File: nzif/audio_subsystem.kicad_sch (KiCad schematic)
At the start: 21 parts, among them J3 AudioJack3, U20 ADAU1761BCPZ, X1 ASE-12.288MHz

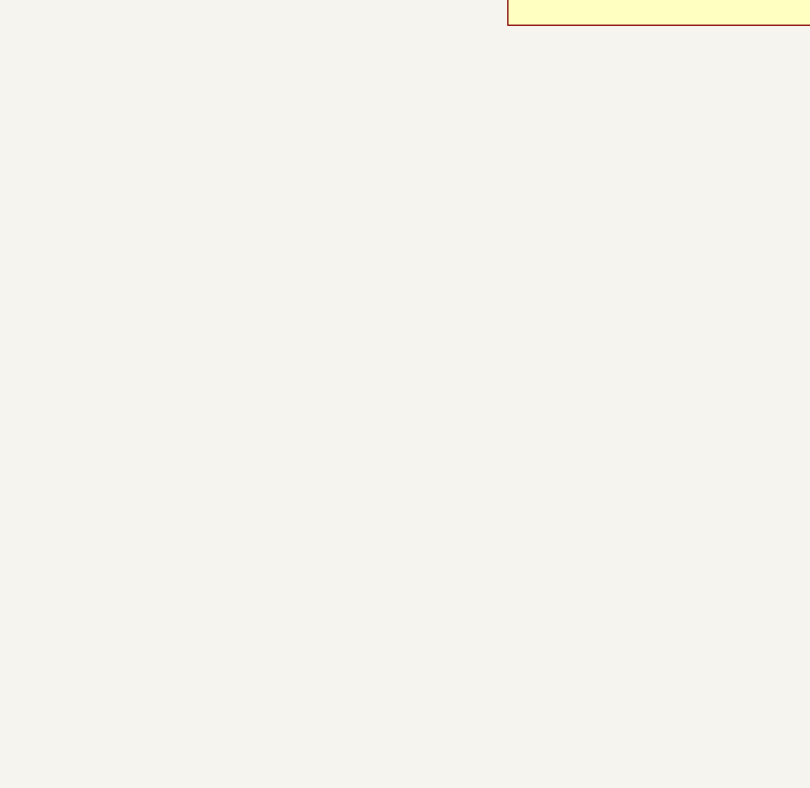
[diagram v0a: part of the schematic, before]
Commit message: add klc compliant 1761
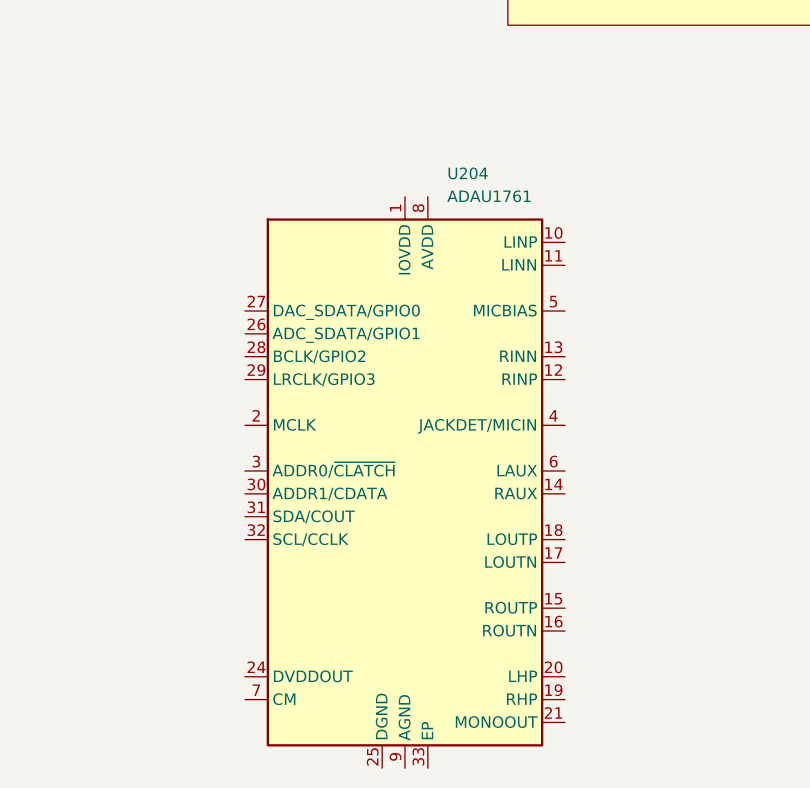
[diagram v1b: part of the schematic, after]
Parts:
- added U204: ADAU1761, Package_CSP:LFCSP-32-1EP_5x5mm_P0.5mm_EP3.5x3.5mm_ThermalVias, symbol Audio:ADAU1761
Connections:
- new net: U204.22 (AGND), U204.9 (AGND)
- new net: U204.23 (AVDD), U204.8 (AVDD)
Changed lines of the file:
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@@
+	)
+	(symbol
+		(lib_id "Audio:ADAU1761")
+		(at 219.71 191.77 0)
+		(unit 1)
+		(exclude_from_sim no)
+		(in_bom yes)
+		(on_board yes)
+		(dnp no)
+		(fields_autoplaced yes)
+		(property "Reference" "U204"
+			(at 224.3933 158.75 0)
+			(effects
+				(font
+					(size 1.27 1.27)
+				)
+				(justify left)
+			)
+		)
+		(property "Value" "ADAU1761"
+			(at 224.3933 161.29 0)
+			(effects
+				(font
+					(size 1.27 1.27)
+				)
+				(justify left)
+			)
+		)
+		(property "Footprint" "Package_CSP:LFCSP-32-1EP_5x5mm_P0.5mm_EP3.5x3.5mm_ThermalVias"
+			(at 219.71 232.918 0)
+			(effects
+				(font
+					(size 1.27 1.27)
+				)
+				(hide yes)
+			)
+		)
+		(property "Datasheet" "https://www.analog.com/media/en/technical-documentation/data-sheets/ADAU1761.pdf"
+			(at 219.71 230.886 0)
+			(effects
+				(font
+					(size 1.27 1.27)
+				)
+				(hide yes)
+			)
+		)
+		(property "Description" "SigmaDSP Stereo, Low Power, 96 kHz, 24-bit Audio Codec with Integrated PLL, VQFN-32 (LFCSP-32)"
+			(at 219.71 228.854 0)
+			(effects
+				(font
+					(size 1.27 1.27)
+				)
+				(hide yes)
+			)
+		)
+		(pin "29"
+		)
+		(pin "3"
+		)
+		(pin "26"
+		)
+		(pin "31"
+		)
+		(pin "28"
+		)
+		(pin "2"
+		)
+		(pin "27"
+		)
+		(pin "30"
+		)
+		(pin "12"
+		)
+		(pin "6"
+		)
+		(pin "22"
+		)
+		(pin "32"
+		)
+		(pin "25"
+		)
+		(pin "1"
+		)
+		(pin "9"
+		)
+		(pin "8"
+		)
+		(pin "11"
+		)
+		(pin "5"
+		)
+		(pin "7"
+		)
+		(pin "24"
+		)
+		(pin "23"
+		)
+		(pin "33"
+		)
+		(pin "10"
+		)
+		(pin "13"
+		)
+		(pin "4"
+		)
+		(pin "17"
+		)
+		(pin "18"
+		)
+		(pin "15"
+		)
+		(pin "16"
+		)
+		(pin "20"
+		)
+		(pin "14"
+		)
+		(pin "21"
+		)
+		(pin "19"
+		)
+		(instances
+			(project ""
+				(path "/fe42ca2f-2bb8-4d5a-9e84-807788ed632f/91ace161-62c2-4ad0-a80e-f8c3c9bc5e50"
+					(reference "U204")
+					(unit 1)
+				)
+			)
+		)
 	)
 	(symbol

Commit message: updated audio subsystem
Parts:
- removed C62, C63, C65, C66, C68, C70: 10u, Capacitor_SMD:C_0805_2012Metric_Pad1.18x1.45mm_HandSolder, symbol Device:C_Polarized_Small_US
- removed C64, C67, C69, C77, C78: 0.1u, Capacitor_SMD:C_0805_2012Metric_Pad1.18x1.45mm_HandSolder, symbol Device:C_Small
- removed C79: 9.1p, Capacitor_SMD:C_0805_2012Metric_Pad1.18x1.45mm_HandSolder, symbol Device:C_Small
- removed C81, C82, C85, C86: 10u, Capacitor_SMD:C_0805_2012Metric_Pad1.18x1.45mm_HandSolder, symbol Device:C_Small
- removed J3: AudioJack3, Connector_Audio:Jack_3.5mm_CUI_SJ-3523-SMT_Horizontal, symbol Connector:AudioJack3
- removed L3: 1.2n, Inductor_SMD:L_0805_2012Metric_Pad1.15x1.40mm_HandSolder, symbol Device:L_Small
- removed R25: 49.9, Resistor_SMD:R_0805_2012Metric_Pad1.20x1.40mm_HandSolder, symbol Device:R_Small_US
- removed U20: ADAU1761BCPZ, Package_DFN_QFN:QFN-32-1EP_5x5mm_P0.5mm_EP3.45x3.45mm, symbol ADAU1761:ADAU1761BCPZ
- removed U204: ADAU1761, Package_CSP:LFCSP-32-1EP_5x5mm_P0.5mm_EP3.5x3.5mm_ThermalVias, symbol Audio:ADAU1761
- removed X1: ASE-12.288MHz, Oscillator:Oscillator_SMD_Abracon_ASE-4Pin_3.2x2.5mm, symbol Oscillator:ASE-xxxMHz
- added C1, C10, C12, C3, C5, C7: 10u, symbol Device:C_Small
- added C11, C15, C16, C2, C4, C6, C8: 0.1u, symbol Device:C_Small
- added C13, C9: 220u, symbol Device:C_Polarized
- added C14: 0.47u, symbol Device:C_Small
- added R1, R4: 49.9k, symbol Device:R_Small_US
- added R2, R6: 10k, symbol Device:R_Small_US
- added R3: 2k, symbol Device:R_Small_US
- added R5: 1k, symbol Device:R_Small_US
- added U1: ADAU1361, Package_CSP:LFCSP-32-1EP_5x5mm_P0.5mm_EP3.5x3.5mm_ThermalVias, symbol Audio:ADAU1361
- added U2: SSM2211S, Package_SO:SOIC-8_3.9x4.9mm_P1.27mm, symbol Amplifier_Audio:SSM2211S
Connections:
- net GND: now also C1.2, C11.1, C15.2, C16.2, C2.2, C3.2, C4.2, C5.2, C6.2, C7.2, C8.2, R1.2, R4.2, U1.22 (AGND), U1.25 (DGND), U1.3 (ADDR0/~{CLATCH}), U1.30 (ADDR1/CDATA), U1.33 (EP), U1.9 (AGND), U2.7 (V-)
- new net: C10.1, U1.11 (LINN)
- new net: C13.1, U1.19 (RHP)
- new net: C14.1, U1.21 (MONOOUT)
- new net: C14.2, R2.1
- new net: C16.1, U2.2 (BYPASS), U2.3 (IN+)
- new net: R2.2, R6.1, U2.4 (IN-)
- new net: C12.1, U1.6 (LAUX)
- new net: C12.2, R4.1, R5.1
- new net: C9.1, U1.20 (LHP)
- new net 3.3V_CODEC: C1.1, C2.1, C3.1, C4.1, U1.1 (IOVDD), U1.23 (AVDD), U1.8 (AVDD)
- new net 5V_Amp: C15.1, U2.6 (V+)
- new net ADC_SDATA: U1.26 (ADC_SDATA)
- new net AMP_SHUTDOWN: U2.1 (SHUTDOWN)
- new net BCLK: U1.28 (BCLK)
- new net CM: C7.1, C8.1, U1.10 (LINP), U1.7 (CM)
- new net DAC_SDATA: U1.27 (DAC_SDATA)
- new net DVDOUT: C5.1, C6.1, U1.24 (DVDDOUT)
- new net Headphone_L: C9.2
- new net Headphone_R: C13.2
- new net LRCLK: U1.29 (LRCLK), U1.32 (SCL/CCLK)
- new net Line_Input: R5.2
- new net Line_Input_ROUTN: U1.16 (ROUTN)
- new net Line_Input_ROUTP: U1.15 (ROUTP)
- new net MCLK: U1.2 (MCLK), U1.31 (SDA/COUT)
- new net MICBIAS: C11.2, R3.1, U1.5 (MICBIAS)
- new net MIC_IN: C10.2, R1.1, R3.2
- new net Speaker+: U2.8 (VoutB)
- new net Speaker-: R6.2, U2.5 (VoutA)
- no-connect marks 1 -> 6
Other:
- note removed: "Audio Codec"
- note removed: "Power Supply Filtering for Codec"

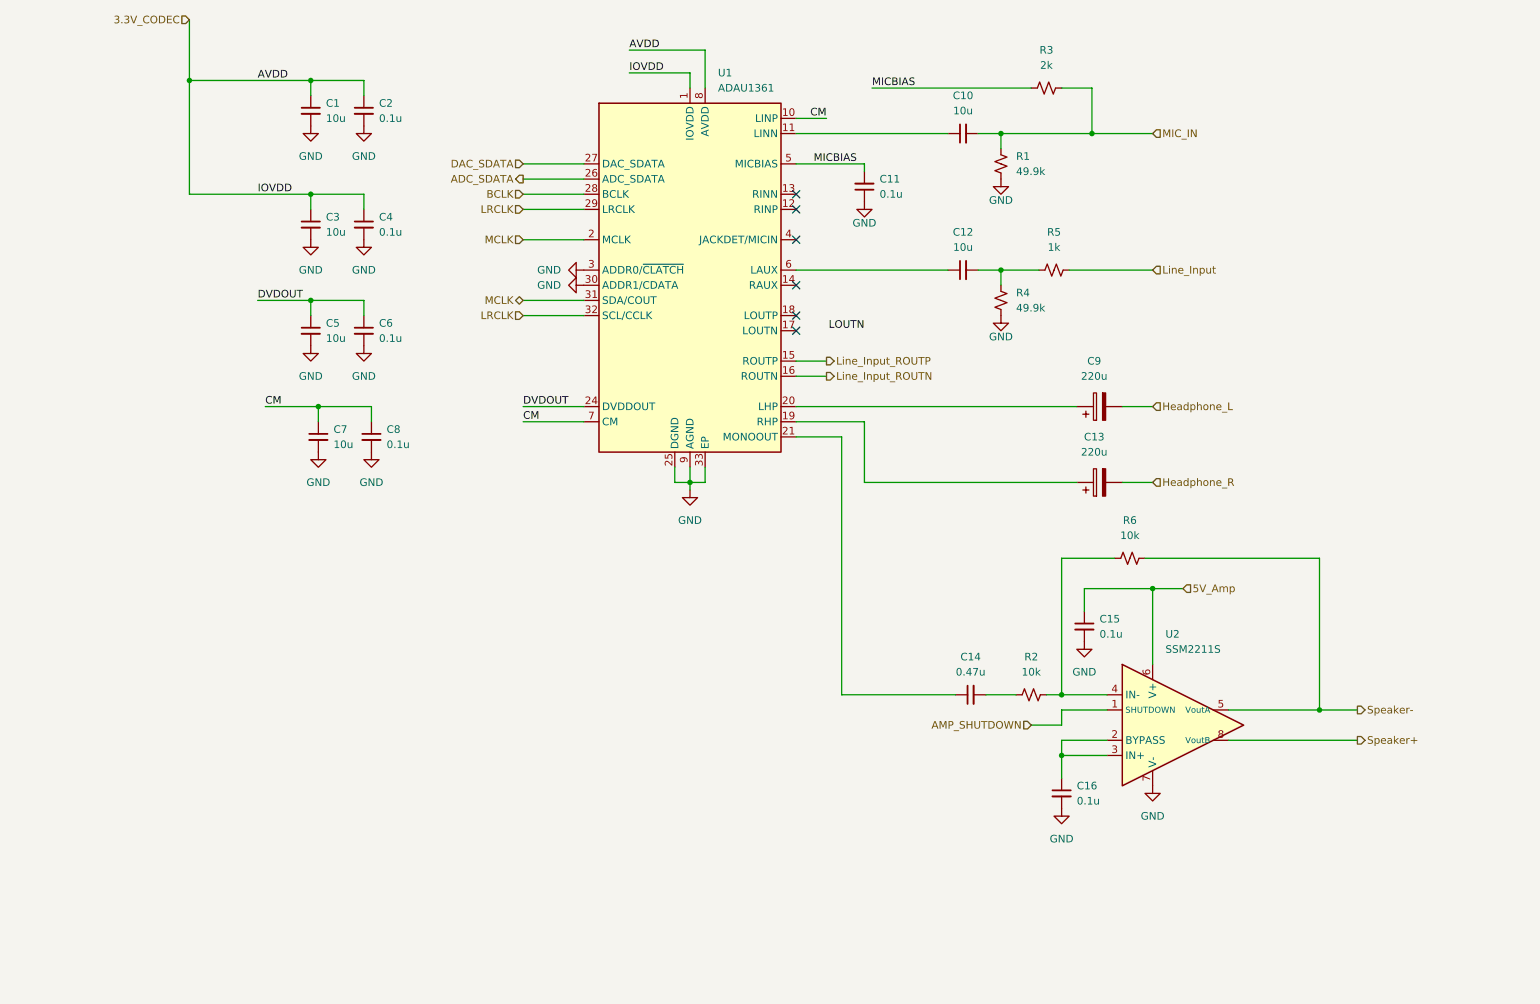
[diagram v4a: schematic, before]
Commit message: reordered sheets - annotate sheets - set all to no sim
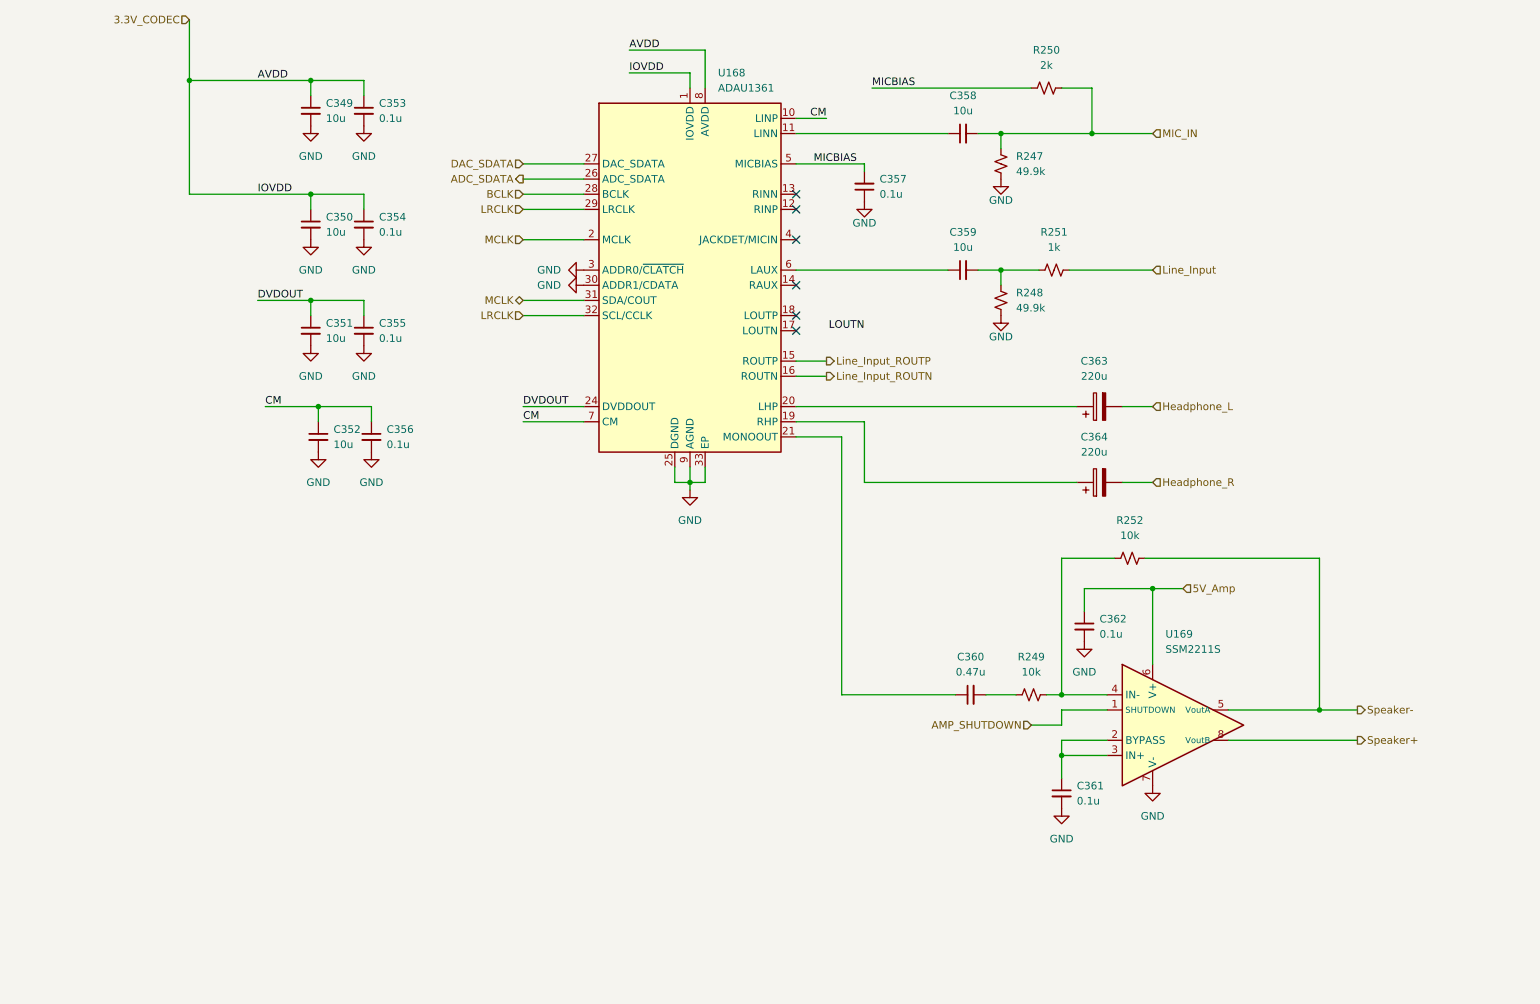
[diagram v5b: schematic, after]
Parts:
- renumbered C1 to C349, C3 to C350, C5 to C351, C7 to C352, C2 to C353, C4 to C354, C6 to C355, C8 to C356, C11 to C357, C10 to C358, C12 to C359, C14 to C360, C16 to C361, C15 to C362, C9 to C363, C13 to C364, R1 to R247, R4 to R248, R2 to R249, R3 to R250, R5 to R251, R6 to R252, U1 to U168, U2 to U169

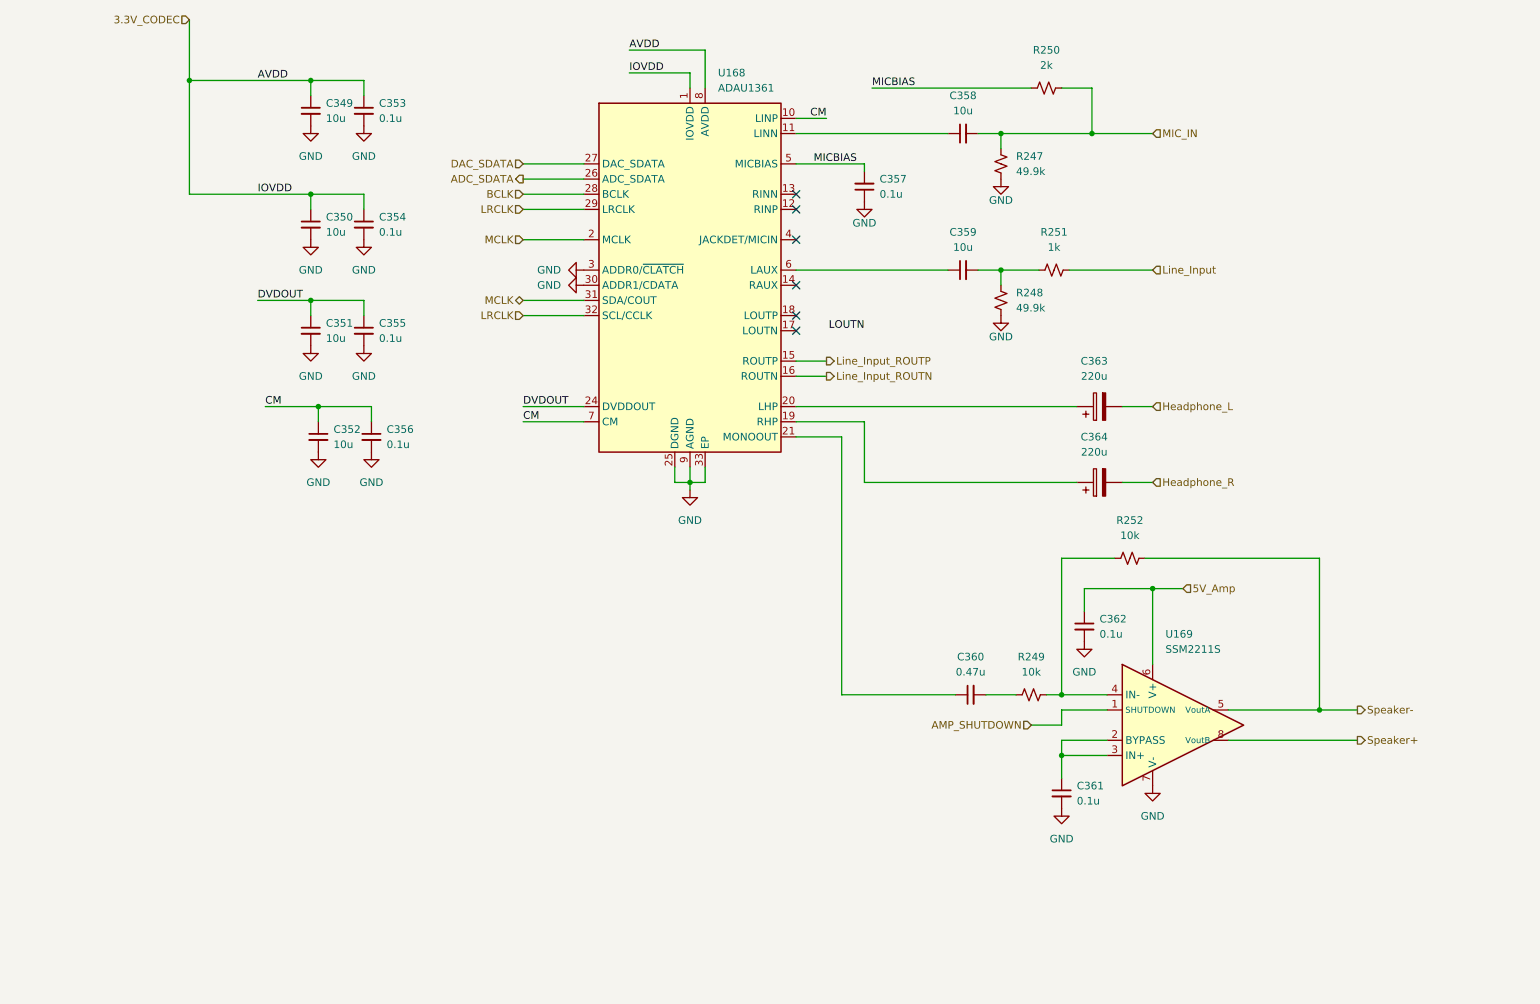
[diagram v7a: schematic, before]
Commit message: add annotations - first run of erc
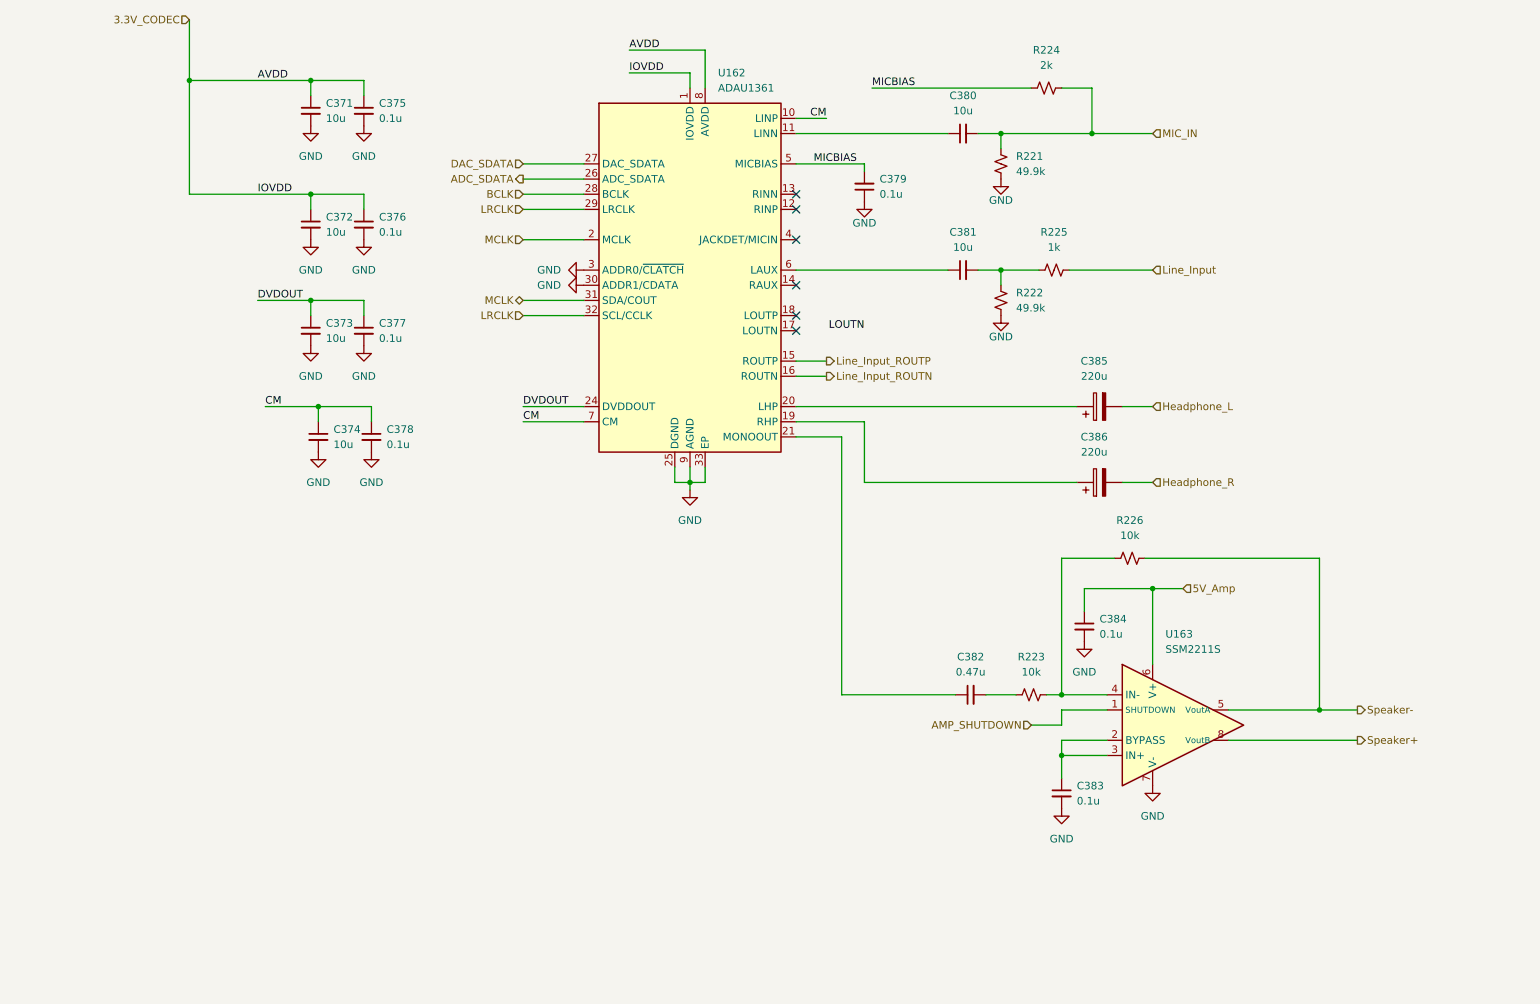
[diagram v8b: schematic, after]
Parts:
- renumbered C349 to C371, C350 to C372, C351 to C373, C352 to C374, C353 to C375, C354 to C376, C355 to C377, C356 to C378, C357 to C379, C358 to C380, C359 to C381, C360 to C382, C361 to C383, C362 to C384, C363 to C385, C364 to C386, R247 to R221, R248 to R222, R249 to R223, R250 to R224, R251 to R225, R252 to R226, U168 to U162, U169 to U163
